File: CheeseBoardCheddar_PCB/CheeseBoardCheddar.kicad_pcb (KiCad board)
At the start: 2 copper layers, 50 x 100 mm, 31 parts, among them P1 USB_Micro, P10 LOGO1, P11 LOGO2, P13 LOGO_CHEESE, P2 5V_EXT, P3 SERIAL_HC12, P4 S_SERIAL, P5 NODEMCU_1, P6 NODEMCU_2, P7 PCB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

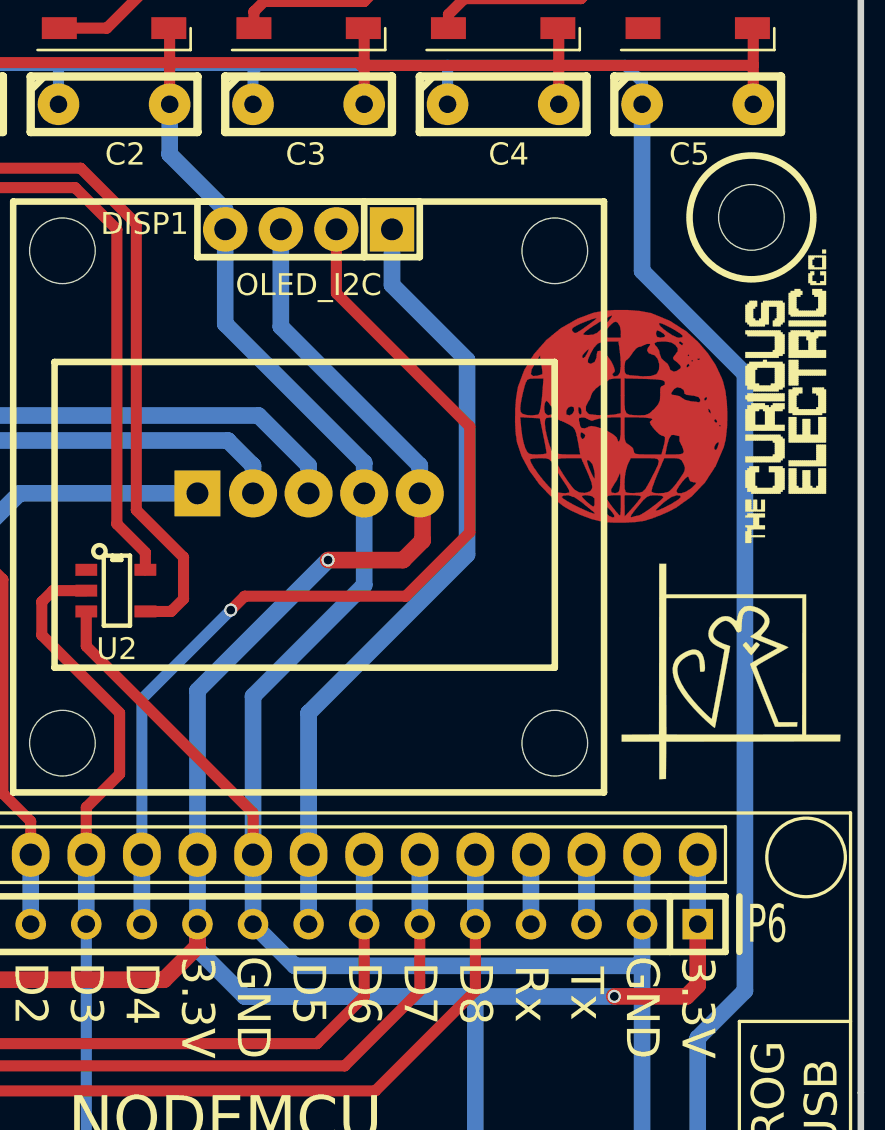
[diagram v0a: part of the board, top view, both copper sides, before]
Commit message: Added I2C bus to PCB
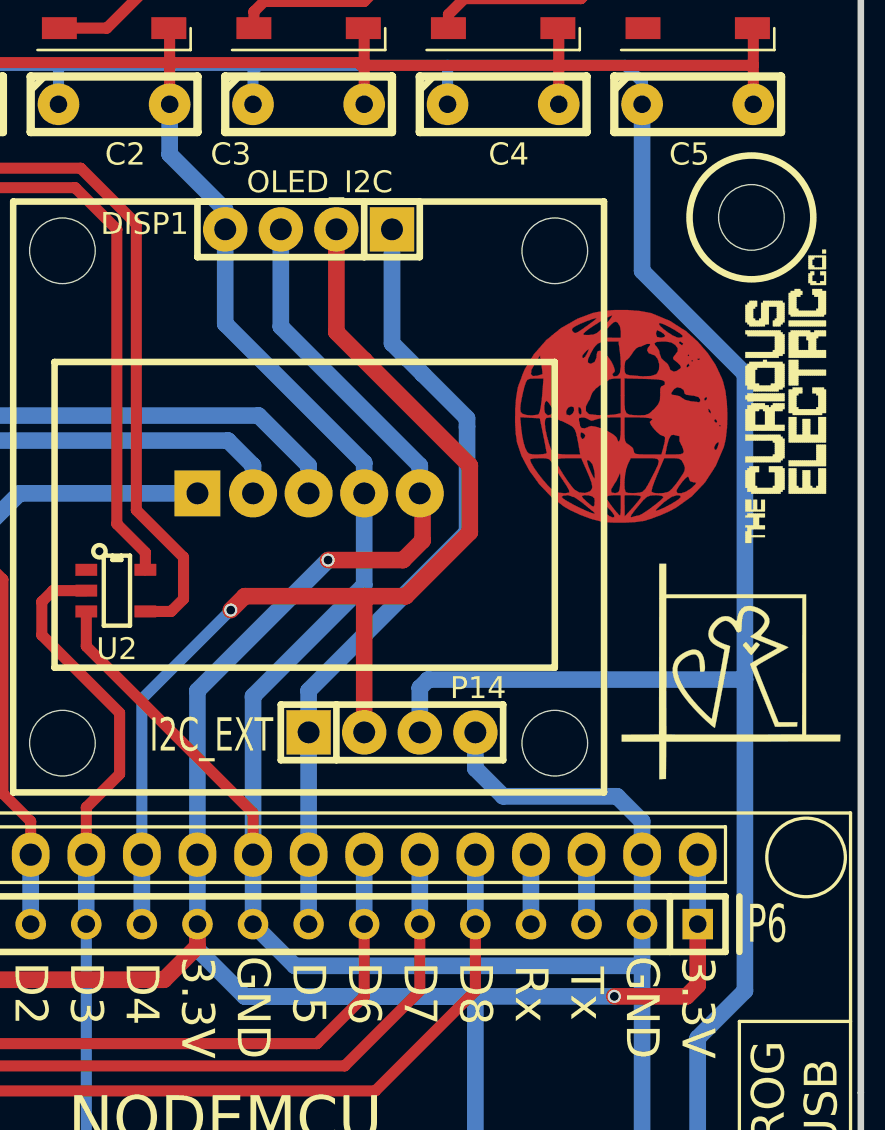
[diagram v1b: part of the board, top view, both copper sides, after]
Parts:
- added P14: I2C_EXT, REInnovationFootprint:SIL-4_large_pad, F.Cu at (117.5, 75.7)
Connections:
- D7 pad 2: Net-(D7-Pad2) -> (no net)
- P1 pad 2: Net-(P1-Pad2) -> (no net)
- P1 pad 3: Net-(P1-Pad3) -> (no net)
- P1 pad 4: Net-(P1-Pad4) -> (no net)
- P10 pad 1: Net-(P10-Pad1) -> (no net)
- U2 pad 1: Net-(U2-Pad1) -> (no net)
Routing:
- net /SCL: track 44.8 -> 63.7 mm
- net /5V_PWR: track 239.8 -> 256.9 mm
- net GND: track 269.3 -> 281.1 mm
- net /SDA: track 36.2 -> 37.1 mm

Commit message: Update of instructions
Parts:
- ENC1: footprint REInnovationFootprint:TH_Encoder -> TH_Encoder
- P14: footprint REInnovationFootprint:SIL-4_large_pad -> matts_components:SIL-5_large_pads_marker
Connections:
- D7 pad 2: (no net) -> Net-(D7-Pad2)
- P1 pad 2: (no net) -> Net-(P1-Pad2)
- P1 pad 3: (no net) -> Net-(P1-Pad3)
- P1 pad 4: (no net) -> Net-(P1-Pad4)
- P10 pad 1: (no net) -> Net-(P10-Pad1)
- P14 pad 1: /SDA -> +3V3
- P14 pad 2: /SCL -> /SDA
- P14 pad 3: /5V_PWR -> /SCL
- P14 pad 4: GND -> /5V_PWR
- U2 pad 1: (no net) -> Net-(U2-Pad1)
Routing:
- net +3V3: track 136.2 -> 151.8 mm
- net GND: track 281.1 -> 283.8 mm
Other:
- board text added: "3.3"
- board text added: "5.0"
- board text added: "SCL"
- board text added: "SDA"
